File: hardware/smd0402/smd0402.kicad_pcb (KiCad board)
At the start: 2 copper layers, 140 x 40 mm, 79 parts, among them J1 Conn_01x04, J2 Conn_01x03, T1 TestPoint_THTPad_3.0x3.0mm_Dr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, T12 TestPoint_THTPad_3.0x3.0mm_Dr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, T13 TestPoint_THTPad_3.0x3.0mm_Dr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, T14 TestPoint_THTPad_3.0x3.0mm_Dr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, T15 TestPoint_THTPad_3.0x3.0mm_Dr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, T16 TestPoint_THTPad_3.0x3.0mm_Dr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, T18 TestPoint_THTPad_3.0x3.0mm_Dr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, T19 TestPoint_THTPad_3.0x3.0mm_Dr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, T20 TestPoint_THTPad_3.0x3.0mm_Dr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, T21 TestPoint_THTPad_3.0x3.0mm_Dr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, T22 TestPoint_THTPad_3.0x3.0mm_Dr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, T42 TestPoint_THTPad_D1.0mm_Drill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, T43 TestPoint_THTPad_D1.0mm_Drill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, T44 TestPoint_THTPad_D1.0mm_Drill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, T45 TestPoint_THTPad_D1.0mm_Drill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, T46 TestPoint_THTPad_D1.0mm_Drill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, T48 TestPoint_THTPad_D1.0mm_Drill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, T49 TestPoint_THTPad_D1.0mm_Drill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, T50 TestPoint_THTPad_D1.0mm_Drill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, T51 TestPoint_THTPad_D1.0mm_Drill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, T51 TestPoint_THTPad_D2.0mm_Drill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, T52 TestPoint_THTPad_D1.0mm_Drill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, T52 TestPoint_THTPad_D2.0mm_Drill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, T53 TestPoint_THTPad_D2.0mm_Drill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, T54 TestPoint_THTPad_D2.0mm_Drill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, T55 TestPoint_THTPad_D2.0mm_Drill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, T56 TestPoint_THTPad_D2.0mm_Drill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, U1 WCH CH32V003F4U6

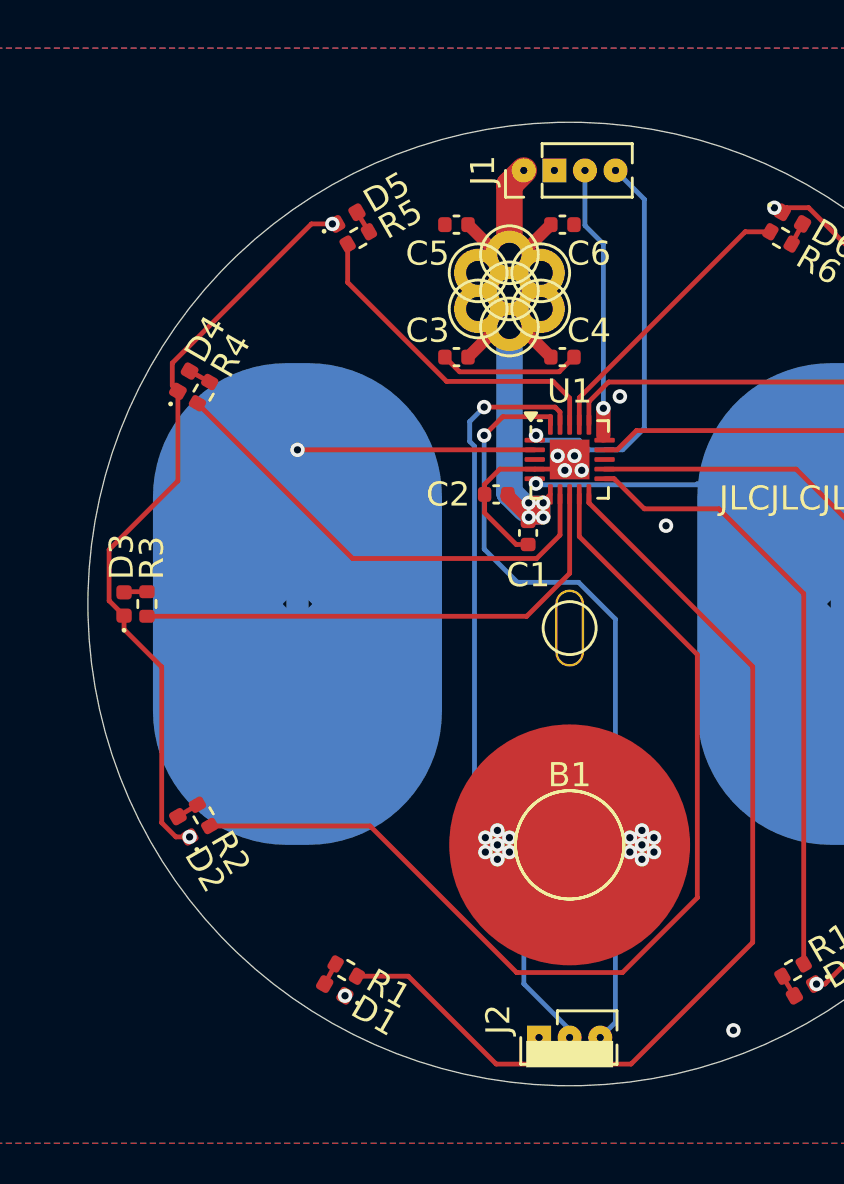
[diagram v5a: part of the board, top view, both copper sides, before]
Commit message: lose NRST, use TIM2 default mapping
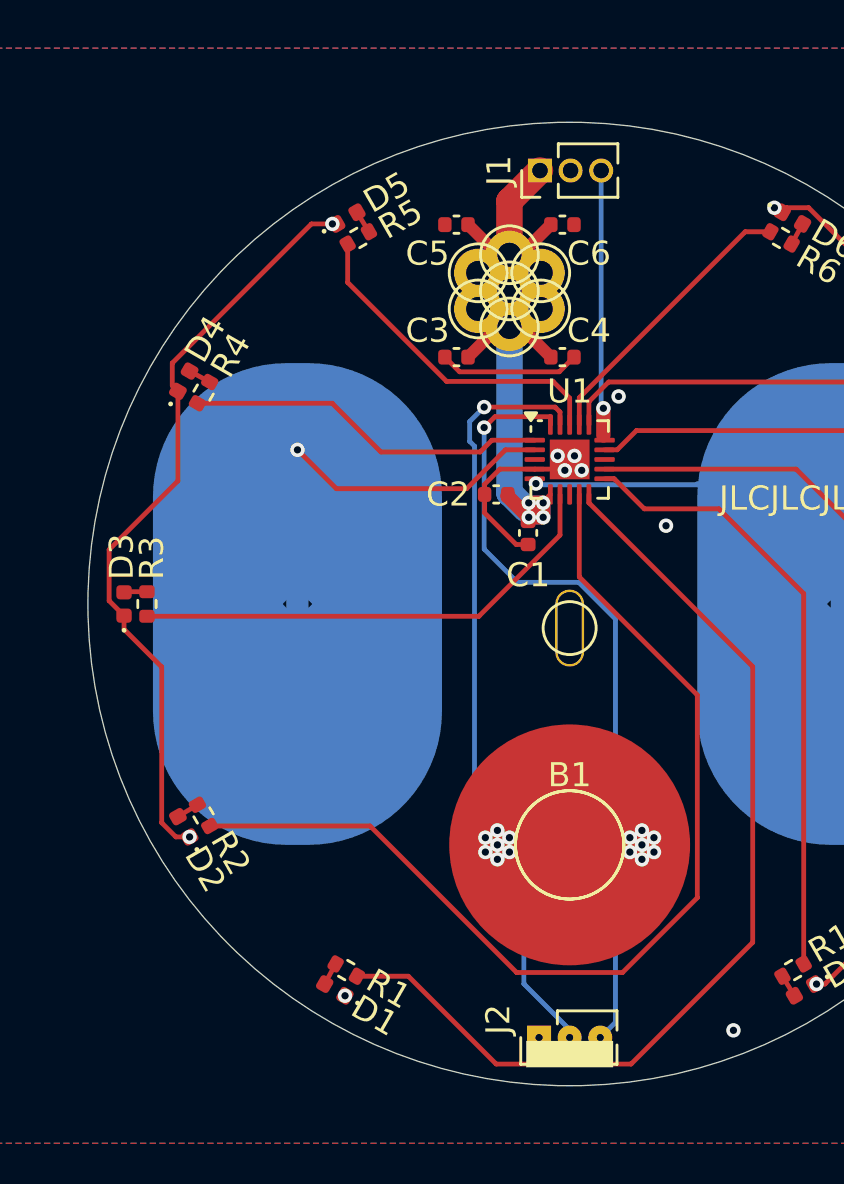
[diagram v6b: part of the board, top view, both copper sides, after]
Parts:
- J1: value Conn_01x04 -> Conn_01x03; footprint Connector_PinHeader_1.27mm:PinHeader_1x04_P1.27mm_Vertical -> Connector_PinHeader_1.27mm:PinHeader_1x03_P1.27mm_Vertical
- moved J1 0.67 mm to (48.8, 32.0)
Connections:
- U1 pad 1: /NRST -> /LED4
- U1 pad 7: /LED4 -> /LED3
- U1 pad 8: /LED3 -> unconnected-(U1-PC1-Pad8)
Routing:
- net /NRST: track 16.5 -> 0.00 mm, vias 1 -> 0
- net /LED4: track 19.8 -> 15.0 mm
- net /touch1: track 9.85 -> 11.2 mm
- net /LED3: track 21.6 -> 20.2 mm

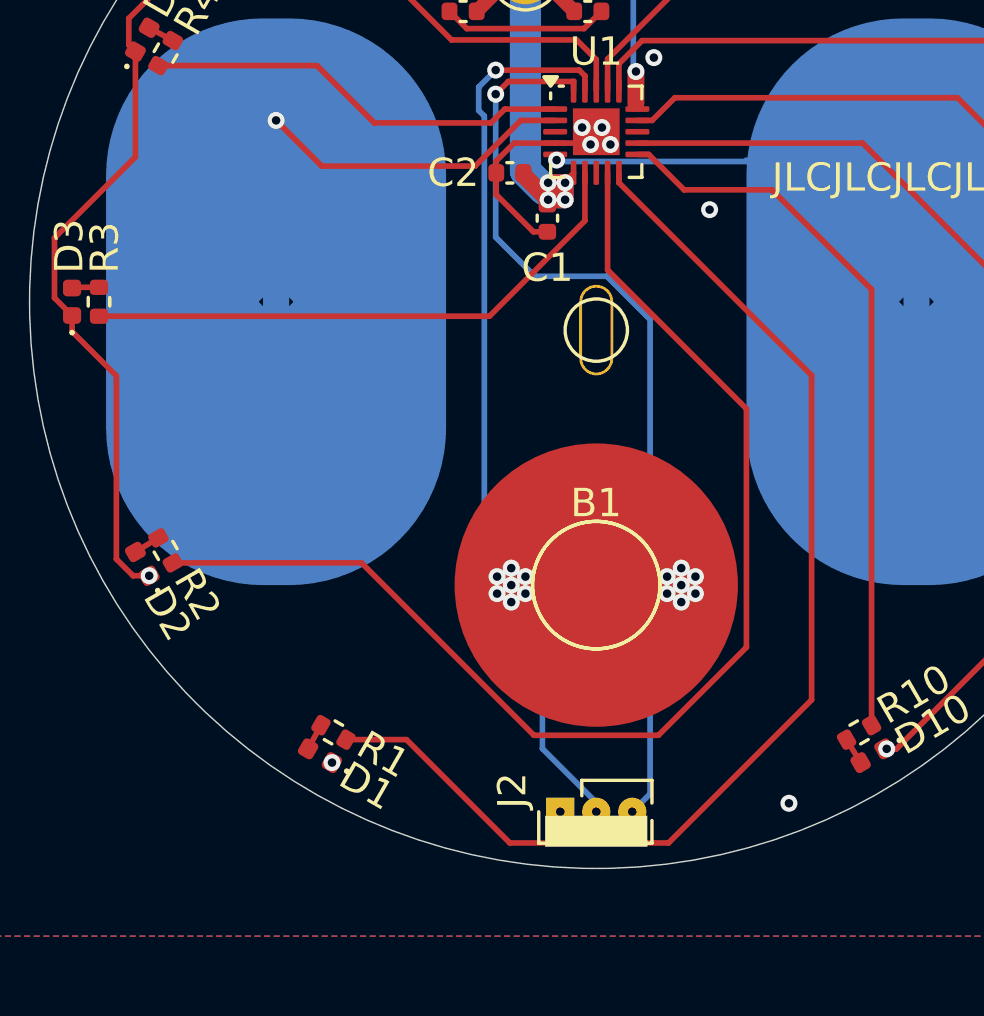
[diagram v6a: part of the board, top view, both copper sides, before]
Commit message: re-route a couple LED signals
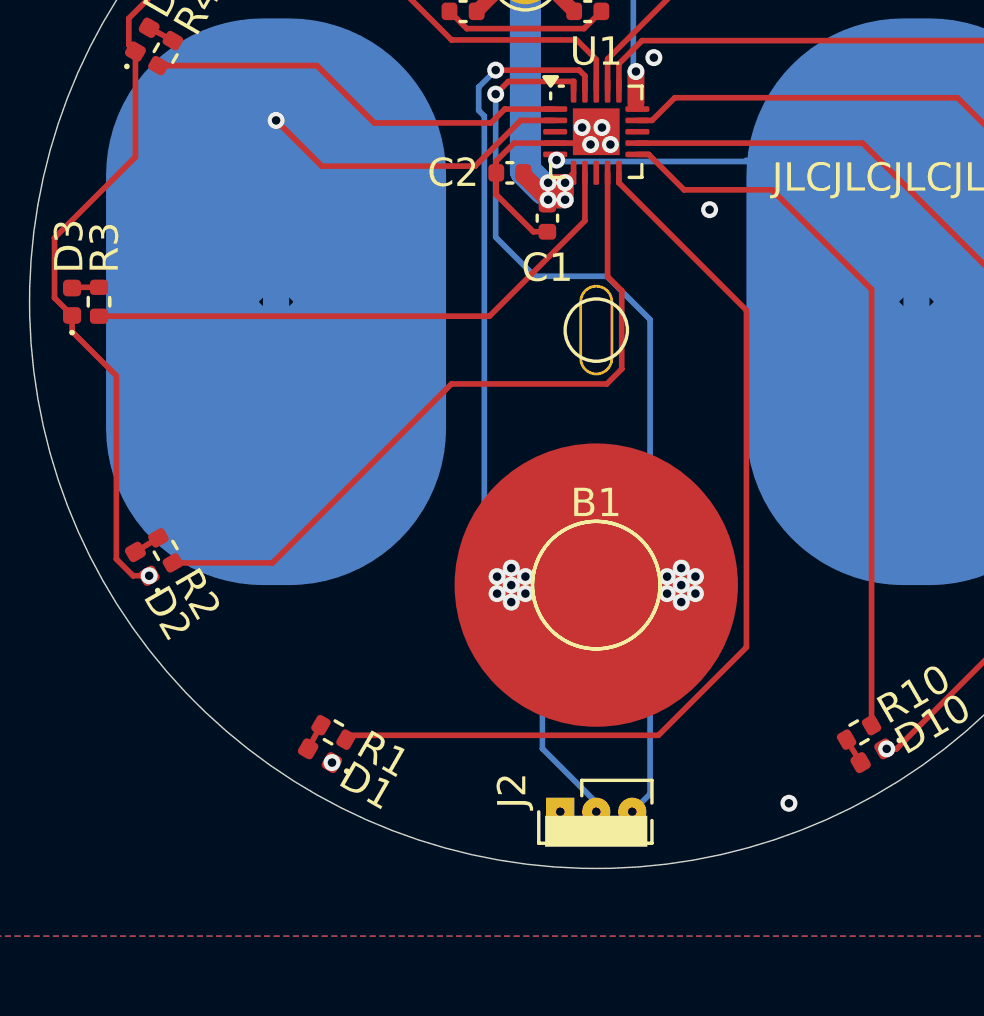
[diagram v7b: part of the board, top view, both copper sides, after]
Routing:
- net /LED2: track 42.8 -> 25.8 mm
- net /LED1: track 41.5 -> 34.1 mm
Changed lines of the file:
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@@
 	)
 	(segment
-		(start 55.3 53.776)
-		(end 50.4 48.876)
+		(start 44.89 52.9)
+		(end 50.372792 52.9)
 		(width 0.2)
 		(layer "F.Cu")
@@
 	)
 	(segment
-		(start 50.4 48.876)
+		(start 50.372792 52.9)
+		(end 50.9 52.372792)
+		(width 0.2)
+		(layer "F.Cu")
+		(net 23)
+	)
+	(segment
+		(start 35.056254 59.216673)
+		(end 38.573327 59.216673)
+		(width 0.2)
+		(layer "F.Cu")
+		(net 23)
+	)
+	(segment
+		(start 50.9 49.609604)
+		(end 50.4 49.109604)
+		(width 0.2)
+		(layer "F.Cu")
+		(net 23)
+	)
+	(segment
+		(start 38.573327 59.216673)
+		(end 44.89 52.9)
+		(width 0.2)
+		(layer "F.Cu")
+		(net 23)
+	)
+	(segment
+		(start 50.9 52.372792)
+		(end 50.9 49.609604)
+		(width 0.2)
+		(layer "F.Cu")
+		(net 23)
+	)
+	(segment
+		(start 50.4 49.109604)
 		(end 50.4 45.45)
 		(width 0.2)
@@
 	)
 	(segment
-		(start 41.716673 59.216673)
-		(end 47.8 65.3)
-		(width 0.2)
-		(layer "F.Cu")
-		(net 23)
-	)
-	(segment
-		(start 47.8 65.3)
+		(start 55.3 62.195332)
 		(end 52.195332 65.3)
 		(width 0.2)
 		(layer "F.Cu")
-		(net 23)
+		(net 24)
 	)
 	(segment
 		(start 52.195332 65.3)
-		(end 55.3 62.195332)
+		(end 41.320418 65.3)
 		(width 0.2)
 		(layer "F.Cu")
-		(net 23)
+		(net 24)
 	)
 	(segment
-		(start 55.3 62.195332)
-		(end 55.3 53.776)
-		(width 0.2)
-		(layer "F.Cu")
-		(net 23)
-	)
-	(segment
-		(start 35.056254 59.216673)
-		(end 41.716673 59.216673)
-		(width 0.2)
-		(layer "F.Cu")
-		(net 23)
-	)
-	(segment
-		(start 43.303745 65.453745)
+		(start 41.320418 65.3)
 		(end 41.166673 65.453745)
 		(width 0.2)
@@
 	)
 	(segment
-		(start 57.6 52.6)
-		(end 57.6 64.05)
-		(width 0.2)
-		(layer "F.Cu")
-		(net 24)
-	)
-	(segment
-		(start 46.95 69.1)
-		(end 43.303745 65.453745)
+		(start 55.3 50.3)
+		(end 55.3 62.195332)
 		(width 0.2)
 		(layer "F.Cu")
@@
 	(segment
 		(start 50.8 45.8)
-		(end 57.6 52.6)
+		(end 55.3 50.3)
 		(width 0.2)
 		(layer "F.Cu")
@@
 		(width 0.2)
 		(layer "F.Cu")
-		(net 24)
-	)
-	(segment
-		(start 57.6 64.05)
-		(end 52.55 69.1)
-		(width 0.2)
-		(layer "F.Cu")
-		(net 24)
-	)
-	(segment
-		(start 52.55 69.1)
-		(end 46.95 69.1)
-		(width 0.2)
-		(layer "F.Cu")
